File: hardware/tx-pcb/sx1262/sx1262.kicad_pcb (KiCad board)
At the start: 2 copper layers, 48 parts, among them J1 Conn_To_J1, J2 Conn_To_J2, Q1 32.0 MHZ, U1 SX1262IMLTRT, U2 PE4259-63

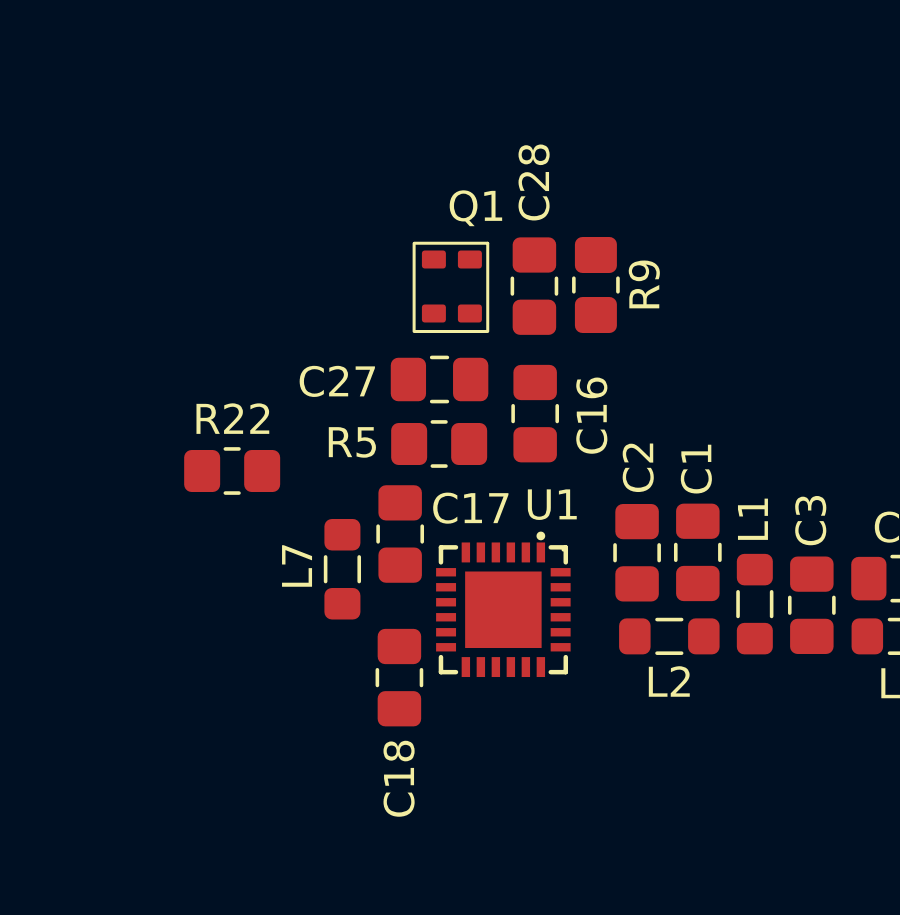
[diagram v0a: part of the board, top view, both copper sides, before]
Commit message: replaced TCXO with a normal 32mhz XTAL
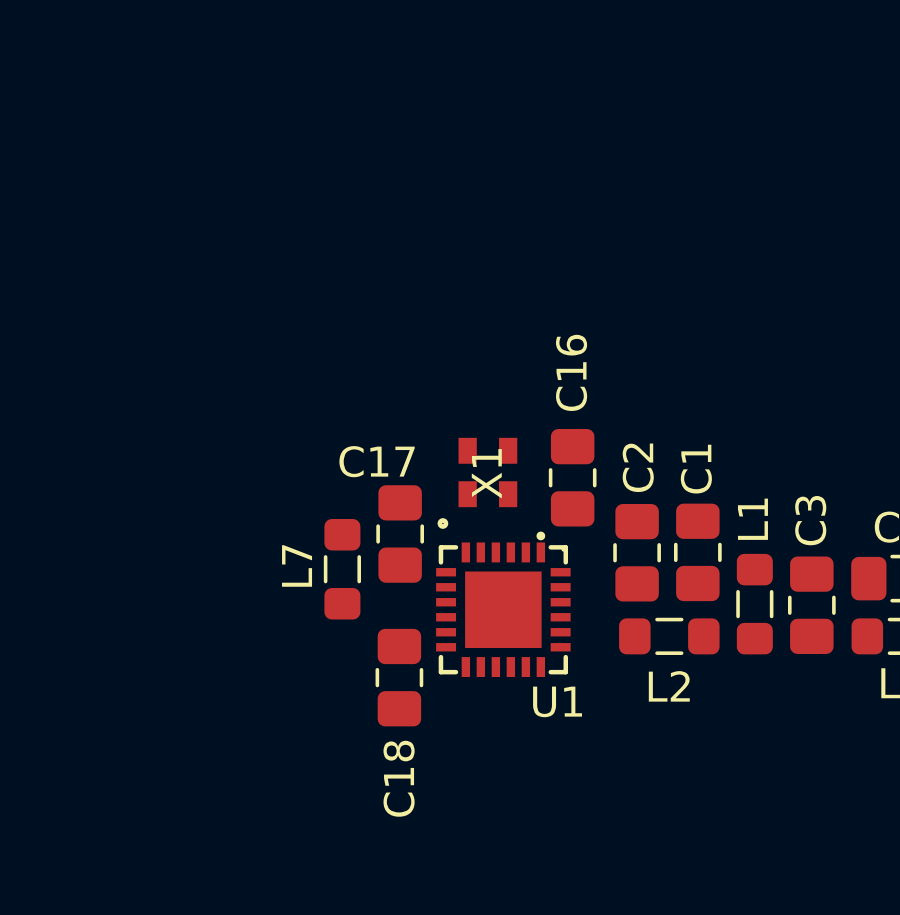
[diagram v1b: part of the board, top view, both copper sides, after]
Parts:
- removed C27: 10p, Capacitor_SMD:C_0805_2012Metric_Pad1.18x1.45mm_HandSolder
- removed C28: 100n, Capacitor_SMD:C_0805_2012Metric_Pad1.18x1.45mm_HandSolder
- removed Q1: 32.0 MHZ, EasyEDA:END4263D_TCXO
- removed R22, R9: 0R, Resistor_SMD:R_0805_2012Metric_Pad1.20x1.40mm_HandSolder
- removed R5: 220R, Resistor_SMD:R_0805_2012Metric_Pad1.20x1.40mm_HandSolder
- added X1: CS11336-32M, rf-lib:NX2016SA_NDK, F.Cu at (153.7, 94.8)
- moved C16 2.48 mm to (156.5, 95.0)
- turned L2 to 0 degrees
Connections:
- C16 pad 1: Net-(U1-VDD_IN) -> +3V3
- U1 pad 1: Net-(U1-VDD_IN) -> +3V3
- U1 pad 4: unconnected-(U1-XTB-Pad4) -> /XTB
- U1 pad 6: Net-(U1-DIO3) -> /DIO3

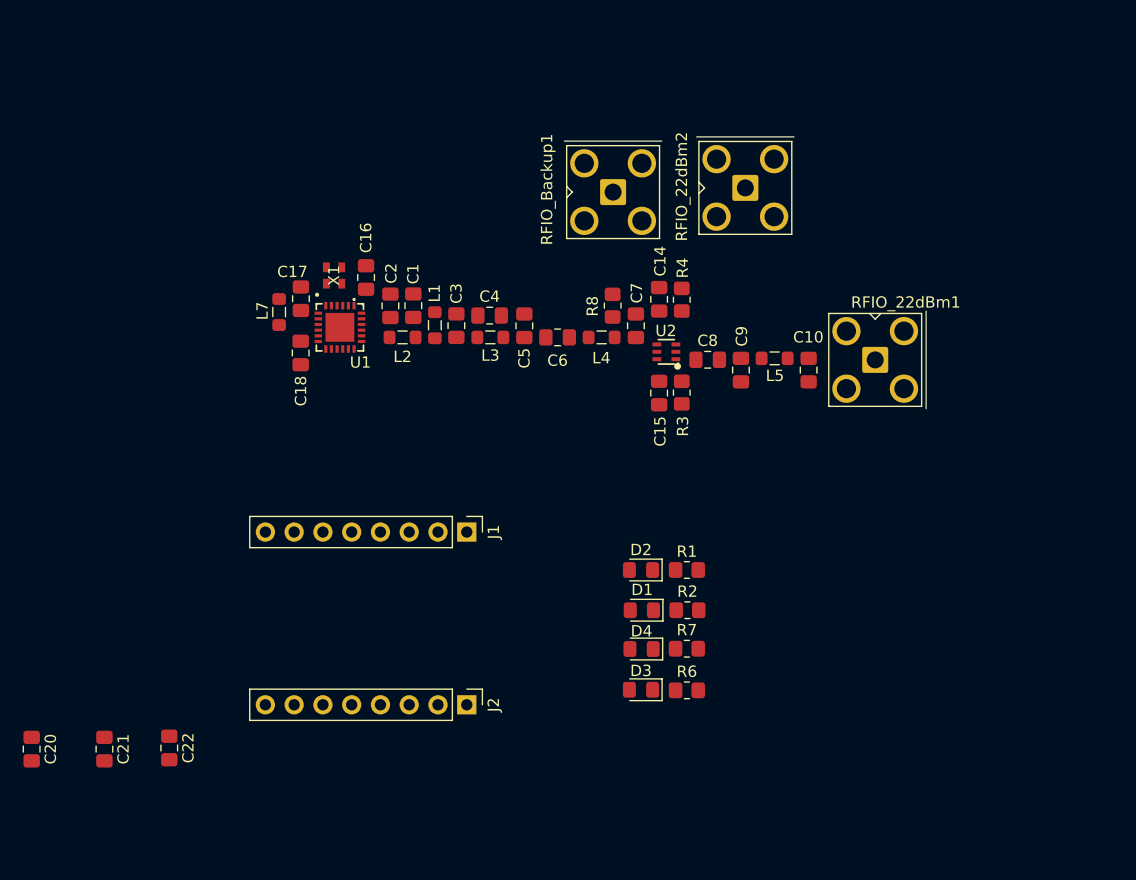
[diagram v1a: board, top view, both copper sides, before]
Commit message: finished sx1262 receiver PCB design
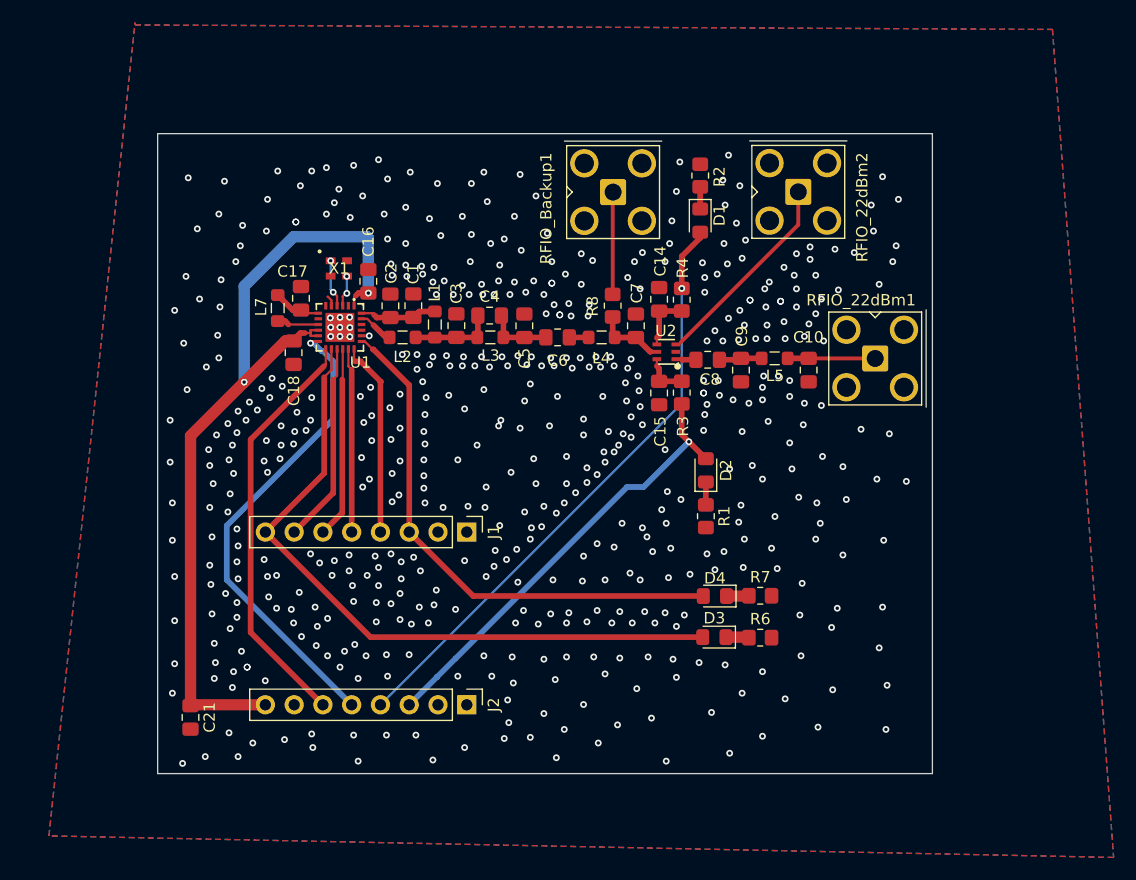
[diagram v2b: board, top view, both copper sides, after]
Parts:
- removed C20: 1u, Capacitor_SMD:C_0805_2012Metric_Pad1.18x1.45mm_HandSolder
- removed C22: 100u, Capacitor_SMD:C_0805_2012Metric_Pad1.18x1.45mm_HandSolder
- moved R2 38.4 mm to (186.0, 86.0), turned to 90 degrees
- moved D1 34.8 mm to (186.0, 90.0), turned to -90 degrees
- moved D2 10.5 mm to (186.5, 112.0), turned to 90 degrees
- moved C21 8.10 mm to (141.0, 133.8)
- moved R7 7.99 mm to (191.3, 123.1)
- moved D4 7.99 mm to (187.3, 123.1)
- moved R6 7.97 mm to (191.3, 126.8)
- moved D3 7.97 mm to (187.2, 126.8)
- moved R1 5.04 mm to (186.5, 116.1), turned to 90 degrees
- moved RFIO_22dBm2 4.69 mm to (194.7, 87.4)
- moved X1 0.76 mm to (154.1, 94.2), turned to 0 degrees
- moved C18 0.63 mm to (150.1, 101.6)
- moved C16 0.39 mm to (156.7, 95.3)
- moved L7 0.37 mm to (148.7, 97.7)
- moved RFIO_22dBm1 0.12 mm to (201.4, 102.2)
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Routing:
- net +3V3: track 0.00 -> 74.8 mm, vias 0 -> 2
- net /BUSY: track 0.00 -> 61.0 mm
- net /RFSW: track 0.00 -> 53.4 mm, vias 0 -> 1
- net /NSS: track 0.00 -> 47.1 mm
- net /DIO2: track 0.00 -> 42.2 mm, vias 0 -> 1
- net /RFSW#: track 0.00 -> 40.3 mm, vias 0 -> 1
- net /DIO1: track 0.00 -> 36.8 mm
- net Net-(RFIO_22dBm2-In): track 0.00 -> 18.1 mm
- net /NRESET: track 0.00 -> 17.7 mm
- net /SCK: track 0.00 -> 17.4 mm
- net /MISO: track 0.00 -> 16.9 mm
- net /MOSI: track 0.00 -> 16.3 mm
- net Net-(RFIO_Backup1-In): track 0.00 -> 9.04 mm
- net Net-(RFIO_22dBm1-In): track 0.00 -> 7.73 mm
- net Net-(C3-Pad1): track 0.00 -> 7.42 mm
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- added copper zone on B.Cu, net GND
- added copper zone on F.Cu, net GND
- added copper zone on In1.Cu, net GND
- added copper zone on In2.Cu, net GND
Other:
- board outline added: 68.4 x 56.5 mm
- copper layers 2 -> 4
